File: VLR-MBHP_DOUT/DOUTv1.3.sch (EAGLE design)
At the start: 20 parts, among them IC2 74HC595, IC3 74HC595, IC4 74HC595

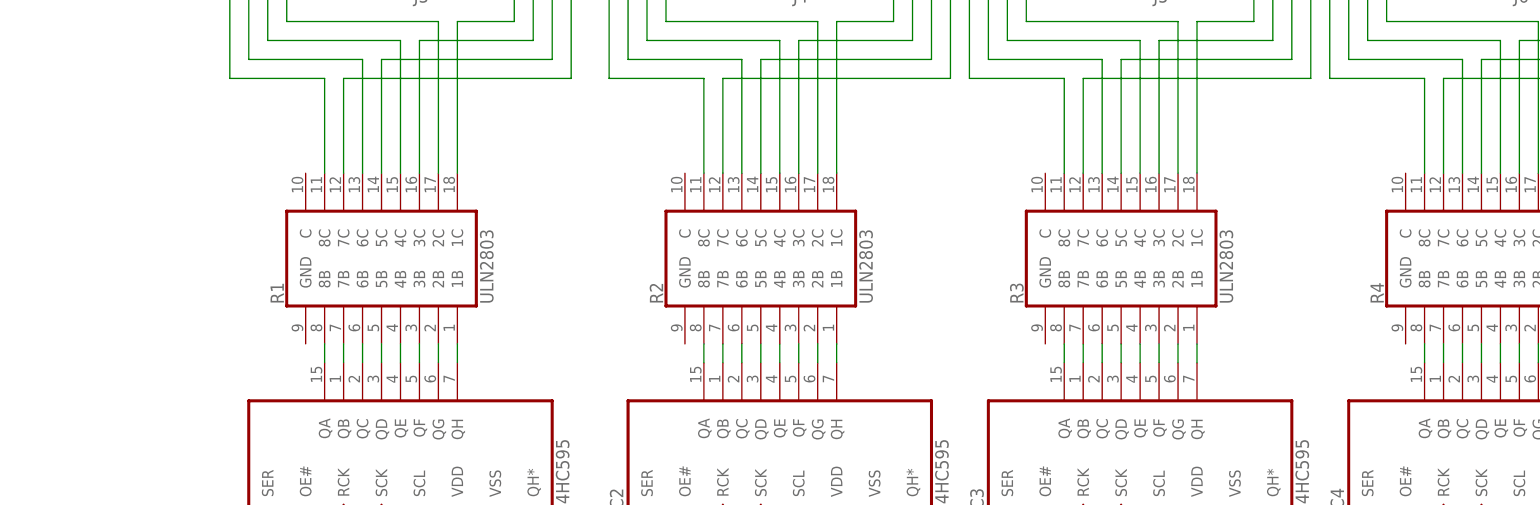
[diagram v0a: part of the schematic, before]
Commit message: D IN/OUT changes
Didn’t get it to a second prototype jet but because of the changes
related to the first prototype im quite shure this works.
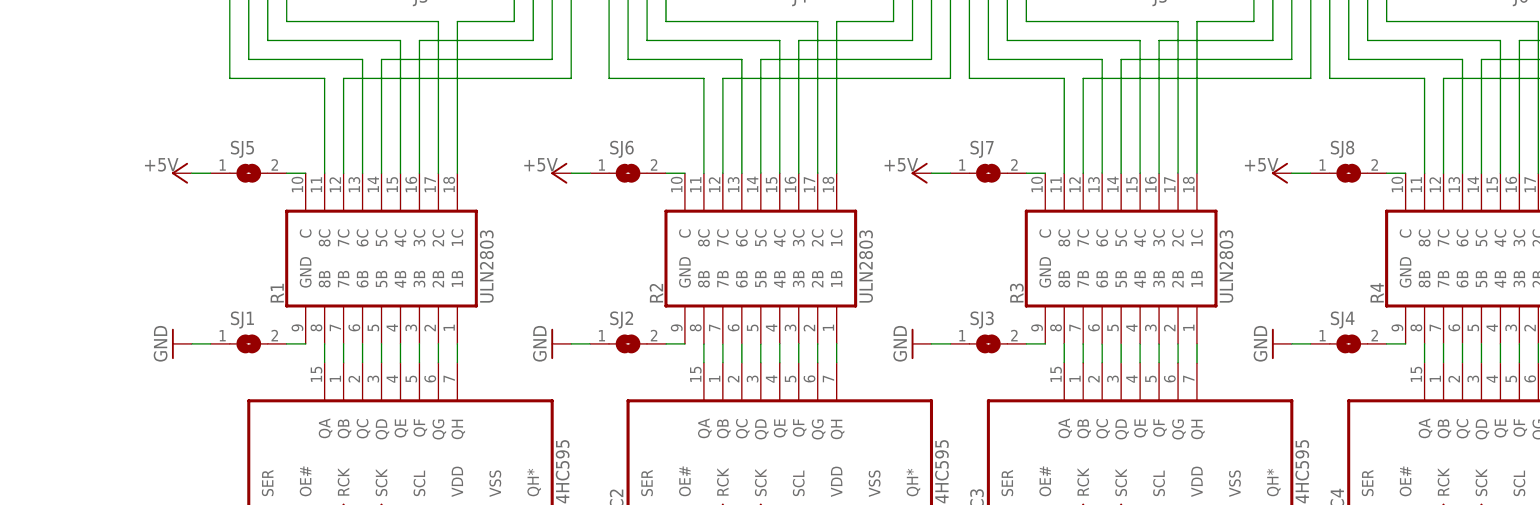
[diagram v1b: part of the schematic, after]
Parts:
- added SJ1, SJ2, SJ3, SJ4, SJ5, SJ6, SJ7, SJ8: (no value), Jumper:SJ
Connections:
- new net N$74: R1.GND, SJ1.2
- new net N$75: R1.C, SJ5.2
- new net N$76: R2.C, SJ6.2
- new net N$77: R2.GND, SJ2.2
- new net N$78: R3.GND, SJ3.2
- new net N$79: R3.C, SJ7.2
- new net N$80: R4.C, SJ8.2
- new net N$81: R4.GND, SJ4.2
- net +5V: now also SJ5.1, SJ6.1, SJ7.1, SJ8.1
- net GND: now also SJ1.1, SJ2.1, SJ3.1, SJ4.1
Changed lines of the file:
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@@
 <?xml version="1.0" encoding="utf-8"?>
 <!DOCTYPE eagle SYSTEM "eagle.dtd">
-<eagle version="6.5.0">
+<eagle version="7.1.0">
 <drawing>
 <settings>
@@
 <part name="P+14" library="supply1" deviceset="+5V" device=""/>
 <part name="GND19" library="supply1" deviceset="GND" device=""/>
+<part name="SJ1" library="Jumper" deviceset="SJ" device=""/>
+<part name="SJ2" library="Jumper" deviceset="SJ" device=""/>
+<part name="SJ3" library="Jumper" deviceset="SJ" device=""/>
+<part name="SJ4" library="Jumper" deviceset="SJ" device=""/>
+<part name="SJ5" library="Jumper" deviceset="SJ" device=""/>
+<part name="SJ6" library="Jumper" deviceset="SJ" device=""/>
+<part name="SJ7" library="Jumper" deviceset="SJ" device=""/>
+<part name="SJ8" library="Jumper" deviceset="SJ" device=""/>
+<part name="P+15" library="supply1" deviceset="+5V" device=""/>
+<part name="P+16" library="supply1" deviceset="+5V" device=""/>
+<part name="P+17" library="supply1" deviceset="+5V" device=""/>
+<part name="P+18" library="supply1" deviceset="+5V" device=""/>
+<part name="GND20" library="supply1" deviceset="GND" device=""/>
+<part name="GND29" library="supply1" deviceset="GND" device=""/>
+<part name="GND30" library="supply1" deviceset="GND" device=""/>
+<part name="GND31" library="supply1" deviceset="GND" device=""/>
 </parts>
 <sheets>
@@
 </instance>
 <instance part="GND19" gate="1" x="276.86" y="68.58" rot="R270"/>
+<instance part="SJ1" gate="1" x="71.12" y="172.72"/>
+<instance part="SJ2" gate="1" x="121.92" y="172.72"/>
+<instance part="SJ3" gate="1" x="170.18" y="172.72"/>
+<instance part="SJ4" gate="1" x="218.44" y="172.72"/>
+<instance part="SJ5" gate="1" x="71.12" y="195.58"/>
+<instance part="SJ6" gate="1" x="121.92" y="195.58"/>
+<instance part="SJ7" gate="1" x="170.18" y="195.58"/>
+<instance part="SJ8" gate="1" x="218.44" y="195.58"/>
+<instance part="P+15" gate="1" x="60.96" y="195.58" smashed="yes" rot="R90">
+<attribute name="VALUE" x="61.722" y="197.612" size="1.778" layer="96" rot="R180"/>
+</instance>
+<instance part="P+16" gate="1" x="111.76" y="195.58" smashed="yes" rot="R90">
+<attribute name="VALUE" x="112.522" y="197.612" size="1.778" layer="96" rot="R180"/>
+</instance>
+<instance part="P+17" gate="1" x="160.02" y="195.58" smashed="yes" rot="R90">
+<attribute name="VALUE" x="160.782" y="197.612" size="1.778" layer="96" rot="R180"/>
+</instance>
+<instance part="P+18" gate="1" x="208.28" y="195.58" smashed="yes" rot="R90">
+<attribute name="VALUE" x="209.042" y="197.612" size="1.778" layer="96" rot="R180"/>
+</instance>
+<instance part="GND20" gate="1" x="60.96" y="172.72" rot="R270"/>
+<instance part="GND29" gate="1" x="111.76" y="172.72" rot="R270"/>
+<instance part="GND30" gate="1" x="160.02" y="172.72" rot="R270"/>
+<instance part="GND31" gate="1" x="208.28" y="172.72" rot="R270"/>
 </instances>
 <busses>
@@
 <pinref part="J7" gate="G$1" pin="1"/>
 <pinref part="GND19" gate="1" pin="GND"/>
+</segment>
+<segment>
+<pinref part="SJ1" gate="1" pin="1"/>
+<pinref part="GND20" gate="1" pin="GND"/>
+<wire x1="66.04" y1="172.72" x2="63.5" y2="172.72" width="0.1524" layer="91"/>
+</segment>
+<segment>
+<pinref part="SJ2" gate="1" pin="1"/>
+<pinref part="GND29" gate="1" pin="GND"/>
+<wire x1="116.84" y1="172.72" x2="114.3" y2="172.72" width="0.1524" layer="91"/>
+</segment>
+<segment>
+<pinref part="SJ3" gate="1" pin="1"/>
+<pinref part="GND30" gate="1" pin="GND"/>
+<wire x1="162.56" y1="172.72" x2="165.1" y2="172.72" width="0.1524" layer="91"/>
+</segment>
+<segment>
+<pinref part="SJ4" gate="1" pin="1"/>
+<pinref part="GND31" gate="1" pin="GND"/>
+<wire x1="210.82" y1="172.72" x2="213.36" y2="172.72" width="0.1524" layer="91"/>
 </segment>
 </net>
@@
 <pinref part="P+14" gate="1" pin="+5V"/>
 </segment>
-</net>
+<segment>
+<pinref part="SJ5" gate="1" pin="1"/>
+<pinref part="P+15" gate="1" pin="+5V"/>
+<wire x1="66.04" y1="195.58" x2="63.5" y2="195.58" width="0.1524" layer="91"/>
+</segment>
+<segment>
+<pinref part="SJ6" gate="1" pin="1"/>
+<pinref part="P+16" gate="1" pin="+5V"/>
+<wire x1="116.84" y1="195.58" x2="114.3" y2="195.58" width="0.1524" layer="91"/>
+</segment>
+<segment>
+<pinref part="SJ7" gate="1" pin="1"/>
+<pinref part="P+17" gate="1" pin="+5V"/>
+<wire x1="162.56" y1="195.58" x2="165.1" y2="195.58" width="0.1524" layer="91"/>
+</segment>
+<segment>
+<pinref part="SJ8" gate="1" pin="1"/>
+<pinref part="P+18" gate="1" pin="+5V"/>
+<wire x1="210.82" y1="195.58" x2="213.36" y2="195.58" width="0.1524" layer="91"/>
+</segment>
+</net>
+<net name="N$74" class="0">
+<segment>
+<pinref part="SJ1" gate="1" pin="2"/>
+<pinref part="R1" gate="IC$1" pin="GND"/>
+<wire x1="76.2" y1="172.72" x2="78.74" y2="172.72" width="0.1524" layer="91"/>
+</segment>
+</net>
+<net name="N$75" class="0">
+<segment>
+<pinref part="SJ5" gate="1" pin="2"/>
+<pinref part="R1" gate="IC$1" pin="C"/>
+<wire x1="76.2" y1="195.58" x2="78.74" y2="195.58" width="0.1524" layer="91"/>
+</segment>
+</net>
+<net name="N$76" class="0">
+<segment>
+<pinref part="SJ6" gate="1" pin="2"/>
+<pinref part="R2" gate="IC$1" pin="C"/>
+<wire x1="127" y1="195.58" x2="129.54" y2="195.58" width="0.1524" layer="91"/>
+</segment>
+</net>
+<net name="N$77" class="0">
+<segment>
+<pinref part="SJ2" gate="1" pin="2"/>
+<pinref part="R2" gate="IC$1" pin="GND"/>
+<wire x1="127" y1="172.72" x2="129.54" y2="172.72" width="0.1524" layer="91"/>
+</segment>
+</net>
+<net name="N$78" class="0">
+<segment>
+<pinref part="SJ3" gate="1" pin="2"/>
+<pinref part="R3" gate="IC$1" pin="GND"/>
+<wire x1="175.26" y1="172.72" x2="177.8" y2="172.72" width="0.1524" layer="91"/>
+</segment>
+</net>
+<net name="N$79" class="0">
+<segment>
+<pinref part="SJ7" gate="1" pin="2"/>
+<pinref part="R3" gate="IC$1" pin="C"/>
+<wire x1="175.26" y1="195.58" x2="177.8" y2="195.58" width="0.1524" layer="91"/>
+</segment>
+</net>
+<net name="N$80" class="0">
+<segment>
+<pinref part="SJ8" gate="1" pin="2"/>
+<pinref part="R4" gate="IC$1" pin="C"/>
+<wire x1="223.52" y1="195.58" x2="226.06" y2="195.58" width="0.1524" layer="91"/>
+</segment>
+</net>
+<net name="N$81" class="0">
+<segment>
+<pinref part="SJ4" gate="1" pin="2"/>
+<pinref part="R4" gate="IC$1" pin="GND"/>
+<wire x1="223.52" y1="172.72" x2="226.06" y2="172.72" width="0.1524" layer="91"/>
+</segment>
+</net>
